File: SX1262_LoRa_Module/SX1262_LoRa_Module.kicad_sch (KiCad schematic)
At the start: 39 parts, among them J1 Conn_01x08_Pin, J2 Conn_01x10_Pin, J3 Conn_01x06_Pin, J4 Conn_01x08_Pin, Q1 32.0Mhz, U1 SX1262IMLTRT, U2 PE4259

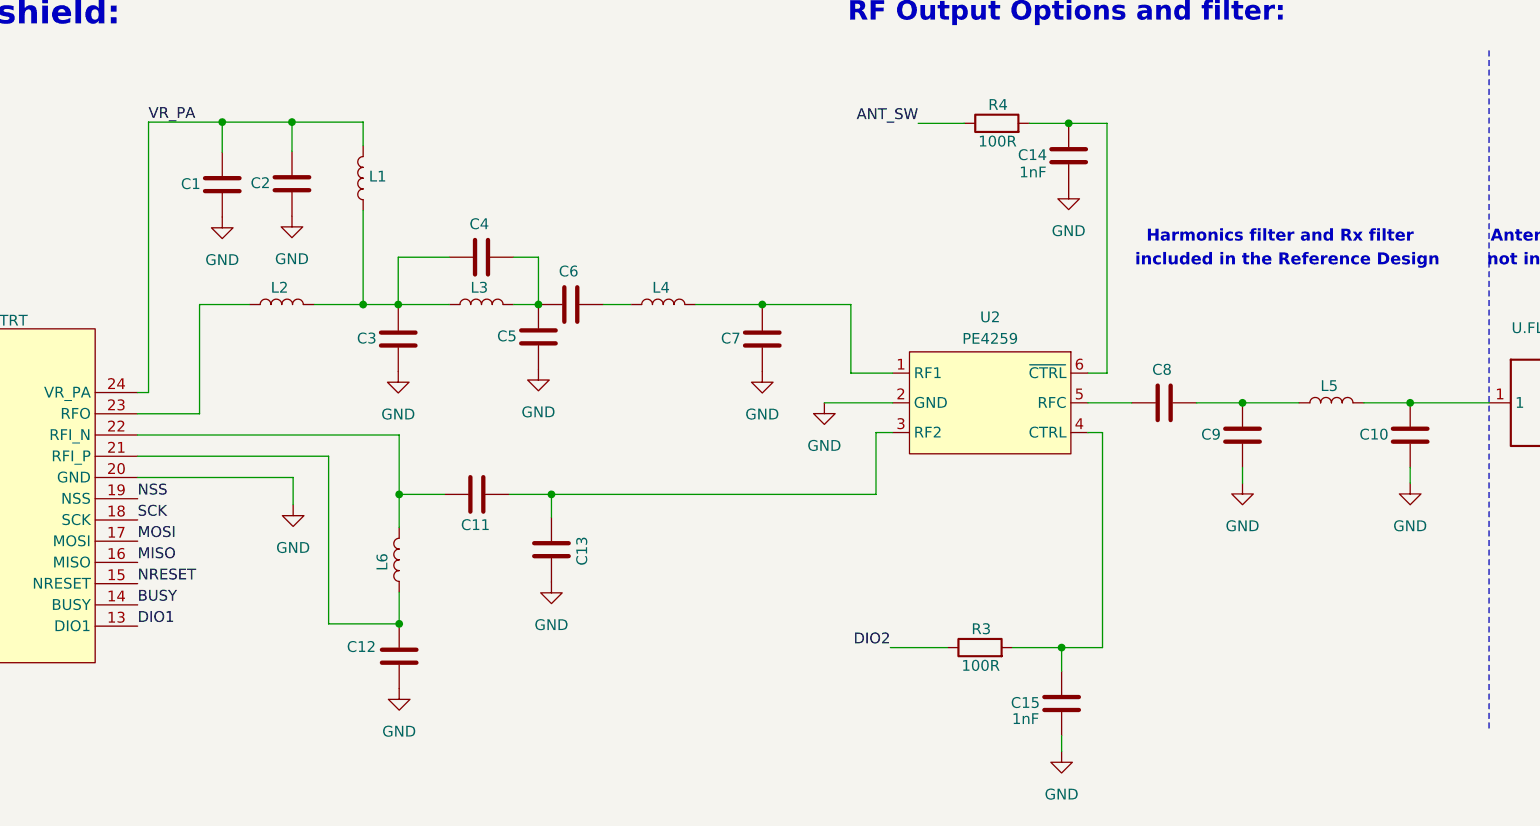
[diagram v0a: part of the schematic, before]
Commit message: -added LC value for the filters
- added values for LC filters based on SEMTECH BOM
- It is recommended to do an 0402 size for the components for the filters , thus following SEMTECH layout size
- Need to note that schemetic here doesnt have yet 0402 footprints designation still contemplating
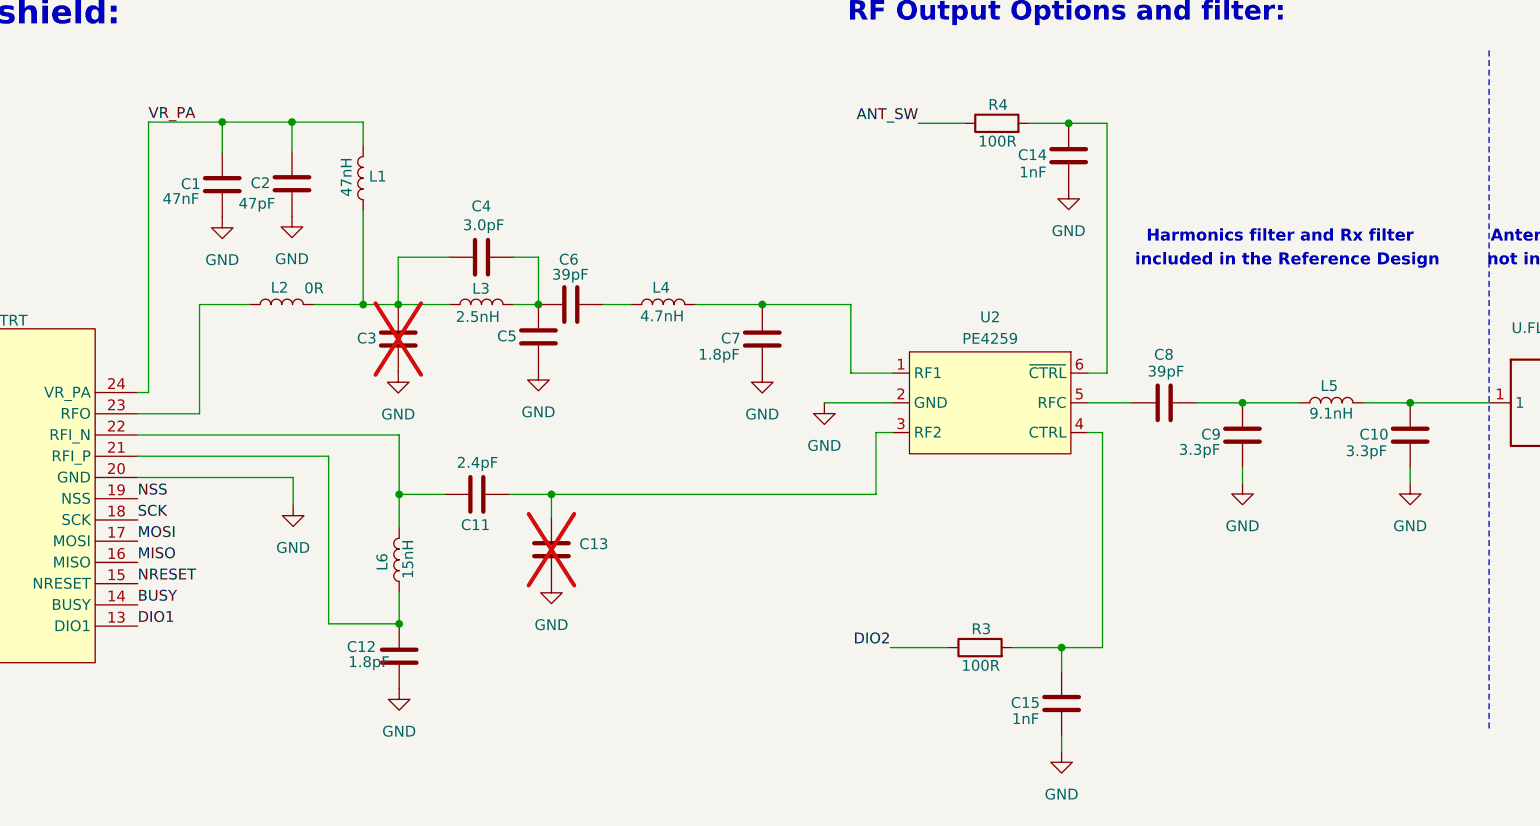
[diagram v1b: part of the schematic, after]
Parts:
- C1: value ~ -> 47nF
- C10, C9: value ~ -> 3.3pF
- C11: value ~ -> 2.4pF
- C12, C7: value ~ -> 1.8pF
- C13, C3: now not fitted
- C2: value ~ -> 47pF
- C4: value ~ -> 3.0pF
- C6, C8: value ~ -> 39pF
- L1: value ~ -> 47nH
- L2: value ~ -> 0R
- L3: value ~ -> 2.5nH
- L4: value ~ -> 4.7nH
- L5: value ~ -> 9.1nH
- L6: value ~ -> 15nH
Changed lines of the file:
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@@
 			)
 		)
-		(property "Value" "~"
+		(property "Value" "1.8pF"
 			(at 209.6668 122.5537 0)
 			(effects
@@
 			)
 		)
-		(property "Value" "~"
-			(at 320.9204 95.1531 0)
+		(property "Value" "3.3pF"
+			(at 312.3157 97.568 0)
 			(effects
 				(font
@@
 		(dnp no)
 		(property "Reference" "C8"
-			(at 304.2977 88.1389 90)
+			(at 304.5224 86.3721 90)
 			(effects
 				(font
@@
 			)
 		)
-		(property "Value" "~"
-			(at 305.0212 86.049 0)
+		(property "Value" "39pF"
+			(at 303.7605 88.3487 90)
 			(effects
 				(font
@@
 			)
 		)
-		(property "Value" "~"
-			(at 250.5509 78.5488 90)
+		(property "Value" "4.7nH"
+			(at 246.6076 81.8426 90)
 			(effects
 				(font
@@
 		(in_bom yes)
 		(on_board yes)
-		(dnp no)
+		(dnp yes)
 		(property "Reference" "C3"
 			(at 212.9982 84.4555 0)
@@
 		(dnp no)
 		(property "Reference" "C6"
-			(at 234.4421 76.5652 90)
+			(at 234.4594 75.1748 90)
 			(effects
 				(font
@@
 			)
 		)
-		(property "Value" "~"
-			(at 235.1656 74.4753 0)
+		(property "Value" "39pF"
+			(at 233.6358 76.9455 90)
 			(effects
 				(font
@@
 			)
 		)
-		(property "Value" "~"
-			(at 225.4841 108.7978 0)
+		(property "Value" "2.4pF"
+			(at 227.3103 99.092 90)
 			(effects
 				(font
@@
 			)
 		)
-		(property "Value" "~"
-			(at 213.7403 106.7047 90)
+		(property "Value" "15nH"
+			(at 216.7012 110.4423 90)
 			(effects
 				(font
@@
 			)
 		)
-		(property "Value" "~"
-			(at 340.6594 95.1531 0)
+		(property "Value" "3.3pF"
+			(at 331.9588 97.7224 0)
 			(effects
 				(font
@@
 			)
 		)
-		(property "Value" "~"
-			(at 200.8062 65.6565 0)
+		(property "Value" "47nF"
+			(at 192.1154 68.0237 0)
 			(effects
 				(font
@@
 		(dnp no)
 		(property "Reference" "L3"
-			(at 225.0829 78.479 90)
+			(at 225.2813 78.6048 90)
 			(effects
 				(font
@@
 			)
 		)
-		(property "Value" "~"
-			(at 229.1511 78.5488 90)
+		(property "Value" "2.5nH"
+			(at 224.9107 81.9198 90)
 			(effects
 				(font
@@
 		(dnp no)
 		(property "Reference" "C4"
-			(at 223.928 70.9967 90)
+			(at 224.1643 68.8948 90)
 			(effects
 				(font
@@
 			)
 		)
-		(property "Value" "~"
-			(at 224.6515 68.9068 0)
+		(property "Value" "3.0pF"
+			(at 223.1554 71.1185 90)
 			(effects
 				(font
@@
 			)
 		)
-		(property "Value" "~"
+		(property "Value" "0R"
 			(at 205.6345 78.5488 90)
 			(effects
@@
 			)
 		)
-		(property "Value" "~"
-			(at 209.0102 65.5485 0)
+		(property "Value" "47pF"
+			(at 201.0633 68.5835 0)
 			(effects
 				(font
@@
 			)
 		)
-		(property "Value" "~"
-			(at 264.3822 83.8365 0)
+		(property "Value" "1.8pF"
+			(at 255.7479 86.3612 0)
 			(effects
 				(font
@@
 		(in_bom yes)
 		(on_board yes)
-		(dnp no)
+		(dnp yes)
 		(property "Reference" "C13"
-			(at 237.1874 107.7624 90)
+			(at 240.2821 108.6664 0)
 			(effects
 				(font
@@
 			)
 		)
-		(property "Value" "~"
-			(at 329.2137 90.1225 90)
+		(property "Value" "9.1nH"
+			(at 325.3877 93.2988 90)
 			(effects
 				(font
@@
 			)
 		)
-		(property "Value" "~"
-			(at 209.4983 61.7701 90)
+		(property "Value" "47nH"
+			(at 209.4589 65.4648 90)
 			(effects
 				(font

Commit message: -layout update
- place footprint per component on schematic
- placed the components on pcb layout based on the evaluation board
- included shiled on the pcb placement
- placed routing on the pcb for the IC and rf switch
- remaining task to deliberate is 10 pins if its either castillated or header
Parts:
- C1, C10, C11, C12, C13, C14, C15, C16, C17, C18, C2, C3, C4, C6, C7, C8, C9: footprint (none) -> Capacitor_SMD:C_0402_1005Metric
- C20: footprint (none) -> Capacitor_SMD:C_0603_1608Metric
- C22: footprint (none) -> Capacitor_SMD:C_0805_2012Metric
- C23: value 10uF -> 100nF; footprint (none) -> Capacitor_SMD:C_0603_1608Metric
- C5: value ~ -> 5.6pF; footprint (none) -> Capacitor_SMD:C_0402_1005Metric
- L1: footprint (none) -> Inductor_SMD:L_0402_1005Metric; LCSC (none) -> C192855
- L2: footprint (none) -> Inductor_SMD:L_0402_1005Metric
- L3: footprint (none) -> Inductor_SMD:L_0402_1005Metric; LCSC (none) -> C703121
- L4: footprint (none) -> Inductor_SMD:L_0402_1005Metric; LCSC (none) -> C98064
- L5: footprint (none) -> Inductor_SMD:L_0402_1005Metric; LCSC (none) -> C6652904
- L6: footprint (none) -> Inductor_SMD:L_0402_1005Metric; LCSC (none) -> C91621
- L7: footprint (none) -> Lora_Footprint_Library:L0805; LCSC (none) -> C383402
- Q1: footprint (none) -> Lora_Footprint_Library:CRYSTAL-SMD_4P-L2.0-W1.6-BL; LCSC (none) -> C1986260
- R1: footprint (none) -> Resistor_SMD:R_0603_1608Metric
- R3, R4: footprint (none) -> Resistor_SMD:R_0402_1005Metric
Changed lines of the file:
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@@
 			)
 		)
-		(property "Footprint" ""
+		(property "Footprint" "Capacitor_SMD:C_0402_1005Metric"
 			(at 125.2082 122.1921 0)
 			(effects
@@
 		)
 		(property "Value" "1.8pF"
-			(at 209.6668 122.5537 0)
+			(at 207.68 122.7986 0)
 			(effects
 				(font
@@
 			)
 		)
-		(property "Footprint" ""
+		(property "Footprint" "Capacitor_SMD:C_0402_1005Metric"
 			(at 216.6157 125.6741 0)
 			(effects
@@
 			)
 		)
-		(property "Footprint" ""
+		(property "Footprint" "Capacitor_SMD:C_0402_1005Metric"
 			(at 313.9715 92.0327 0)
 			(effects
@@
 			)
 		)
-		(property "Footprint" ""
+		(property "Footprint" "Capacitor_SMD:C_0402_1005Metric"
 			(at 138.8917 82.3903 0)
 			(effects
@@
 			)
 		)
-		(property "Footprint" ""
+		(property "Footprint" "Capacitor_SMD:C_0402_1005Metric"
 			(at 301.9008 92.9979 0)
 			(effects
@@
 			)
 		)
-		(property "Footprint" ""
+		(property "Footprint" "Inductor_SMD:L_0402_1005Metric"
 			(at 246.7409 80.459 0)
 			(effects
@@
 			)
 		)
+		(property "LCSC" "C98064"
+			(at 246.7409 80.459 90)
+			(effects
+				(font
+					(size 1.27 1.27)
+				)
+				(hide yes)
+			)
+		)
 		(pin "2"
 		)
@@
 			)
 		)
-		(property "Footprint" ""
+		(property "Footprint" "Capacitor_SMD:C_0402_1005Metric"
 			(at 214.5764 80.7161 0)
 			(effects
@@
 			)
 		)
-		(property "Footprint" ""
+		(property "Footprint" "Capacitor_SMD:C_0402_1005Metric"
 			(at 232.0452 81.4242 0)
 			(effects
@@
 			)
 		)
-		(property "Footprint" ""
+		(property "Footprint" "Capacitor_SMD:C_0402_1005Metric"
 			(at 228.6045 101.8489 0)
 			(effects
@@
 			)
 		)
-		(property "Footprint" ""
+		(property "Footprint" "Capacitor_SMD:C_0402_1005Metric"
 			(at 113.0597 122.2721 0)
 			(effects
@@
 			)
 		)
-		(property "Footprint" ""
+		(property "Footprint" "Inductor_SMD:L_0402_1005Metric"
 			(at 215.6505 110.5147 0)
 			(effects
@@
 			)
 		)
+		(property "LCSC" "C91621"
+			(at 215.6505 110.5147 90)
+			(effects
+				(font
+					(size 1.27 1.27)
+				)
+				(hide yes)
+			)
+		)
 		(pin "2"
 		)
@@
 			)
 		)
-		(property "Footprint" ""
+		(property "Footprint" "Capacitor_SMD:C_0402_1005Metric"
 			(at 333.7105 92.0327 0)
 			(effects
@@
 			)
 		)
-		(property "Footprint" ""
+		(property "Footprint" "Capacitor_SMD:C_0402_1005Metric"
 			(at 193.8573 62.5361 0)
 			(effects
@@
 			)
 		)
-		(property "Footprint" ""
+		(property "Footprint" "Inductor_SMD:L_0402_1005Metric"
 			(at 225.3411 80.459 0)
 			(effects
@@
 			)
 		)
+		(property "LCSC" "C703121"
+			(at 225.3411 80.459 90)
+			(effects
+				(font
+					(size 1.27 1.27)
+				)
+				(hide yes)
+			)
+		)
 		(pin "2"
 		)
@@
 			)
 		)
-		(property "Footprint" ""
+		(property "Footprint" "Capacitor_SMD:C_0402_1005Metric"
 			(at 221.5311 75.8557 0)
 			(effects
@@
 			)
 		)
-		(property "Value" "~"
-			(at 238.0289 83.5794 0)
+		(property "Value" "5.6pF"
+			(at 229.3628 86.0393 0)
 			(effects
 				(font
@@
 			)
 		)
-		(property "Footprint" ""
+		(property "Footprint" "Capacitor_SMD:C_0402_1005Metric"
 			(at 231.08 80.459 0)
 			(effects
@@
 			)
 		)
-		(property "Footprint" ""
+		(property "Footprint" "Capacitor_SMD:C_0805_2012Metric"
 			(at 185.9707 220.9317 0)
 			(effects
@@
 			)
 		)
-		(property "Footprint" ""
+		(property "Footprint" "Inductor_SMD:L_0402_1005Metric"
 			(at 201.8245 80.459 0)
 			(effects
@@
 			)
 		)
-		(property "Footprint" ""
+		(property "Footprint" "Resistor_SMD:R_0402_1005Metric"
 			(at 284.0346 122.6261 90)
 			(effects
@@
 		(dnp no)
 		(property "Reference" "C23"
-			(at 189.1592 216.0317 0)
+			(at 189.2131 216.2264 0)
 			(effects
 				(font
@@
 			)
 		)
-		(property "Value" "10uF"
-			(at 188.2817 218.0114 0)
+		(property "Value" "100nF"
+			(at 187.1998 218.4215 0)
 			(effects
 				(font
@@
 			)
 		)
-		(property "Footprint" ""
+		(property "Footprint" "Capacitor_SMD:C_0603_1608Metric"
 			(at 196.286 220.9317 0)
 			(effects
@@
 			)
 		)
-		(property "Footprint" ""
+		(property "Footprint" "Capacitor_SMD:C_0402_1005Metric"
 			(at 202.0613 62.4281 0)
 			(effects
@@
 			)
 		)
-		(property "Footprint" ""
+		(property "Footprint" "Lora_Footprint_Library:L0805"
 			(at 124.3611 109.5967 0)
 			(effects
@@
 			)
 		)
+		(property "LCSC" "C383402"
+			(at 124.3611 109.5967 90)
+			(effects
+				(font
+					(size 1.27 1.27)
+				)
+				(hide yes)
+			)
+		)
 		(pin "2"
 		)
@@
 			)
 		)
-		(property "Footprint" ""
+		(property "Footprint" "Resistor_SMD:R_0603_1608Metric"
 			(at 209.3951 215.0897 90)
 			(effects
@@
 			)
 		)
-		(property "Footprint" ""
+		(property "Footprint" "Capacitor_SMD:C_0402_1005Metric"
 			(at 257.4333 80.7161 0)
 			(effects
@@
 			)
 		)
+		(property "LCSC" ""
+			(at 258.3985 84.5261 0)
+			(effects
+				(font
+					(size 1.27 1.27)
+				)
+				(hide yes)
+			)
+		)
 		(pin "2"
 		)
@@
 			)
 		)
-		(property "Footprint" ""
+		(property "Footprint" "Resistor_SMD:R_0402_1005Metric"
 			(at 286.0085 60.9041 90)
 			(effects
@@
 			)
 		)
-		(property "Footprint" ""
+		(property "Footprint" "Capacitor_SMD:C_0402_1005Metric"
 			(at 232.6111 105.5119 0)
 			(effects
@@
 			)
 		)
-		(property "Footprint" ""
+		(property "Footprint" "Capacitor_SMD:C_0402_1005Metric"
 			(at 292.6732 123.6219 0)
 			(effects
@@
 			)
 		)
-		(property "Footprint" ""
+		(property "Footprint" "Capacitor_SMD:C_0603_1608Metric"
 			(at 224.6013 220.9317 0)
 			(effects
@@
 			)
 		)
-		(property "Footprint" ""
+		(property "Footprint" "Inductor_SMD:L_0402_1005Metric"
 			(at 325.4037 92.0327 0)
 			(effects
@@
 			)
 		)
+		(property "LCSC" "C6652904"
+			(at 325.4037 92.0327 90)
+			(effects
+				(font
+					(size 1.27 1.27)
+				)
+				(hide yes)
+			)
+		)
 		(pin "2"
 		)
@@
 			)
 		)
-		(property "Footprint" ""
+		(property "Footprint" "Inductor_SMD:L_0402_1005Metric"
 			(at 211.4085 65.5801 0)
 			(effects
@@
 			)
 		)
+		(property "LCSC" "C192855"
+			(at 211.4085 65.5801 0)
+			(effects
+				(font
+					(size 1.27 1.27)
+				)
+				(hide yes)
+			)
+		)
 		(pin "2"
 		)
@@
 			)
 		)
-		(property "Footprint" ""
+		(property "Footprint" "Capacitor_SMD:C_0402_1005Metric"
 			(at 293.5039 59.1261 0)
 			(effects
@@
 			)
 		)
+		(property "Field5" ""
+			(at 294.4691 62.9361 0)
+			(effects
+				(font
+					(size 1.27 1.27)
+				)
+				(hide yes)
+			)
+		)
 		(pin "2"
 		)
@@
 			)
 		)
-		(property "Footprint" ""
+		(property "Footprint" "Lora_Footprint_Library:CRYSTAL-SMD_4P-L2.0-W1.6-BL"
 			(at 117.9616 65.9881 0)
 			(effects
@@
 			(at 117.9616 65.9881 0)
 			(effects
+				(font
+					(size 1.27 1.27)
+				)
+				(hide yes)
+			)
+		)
+		(property "LCSC" "C1986260"
+			(at 117.9616 65.9881 0)
+			(effects

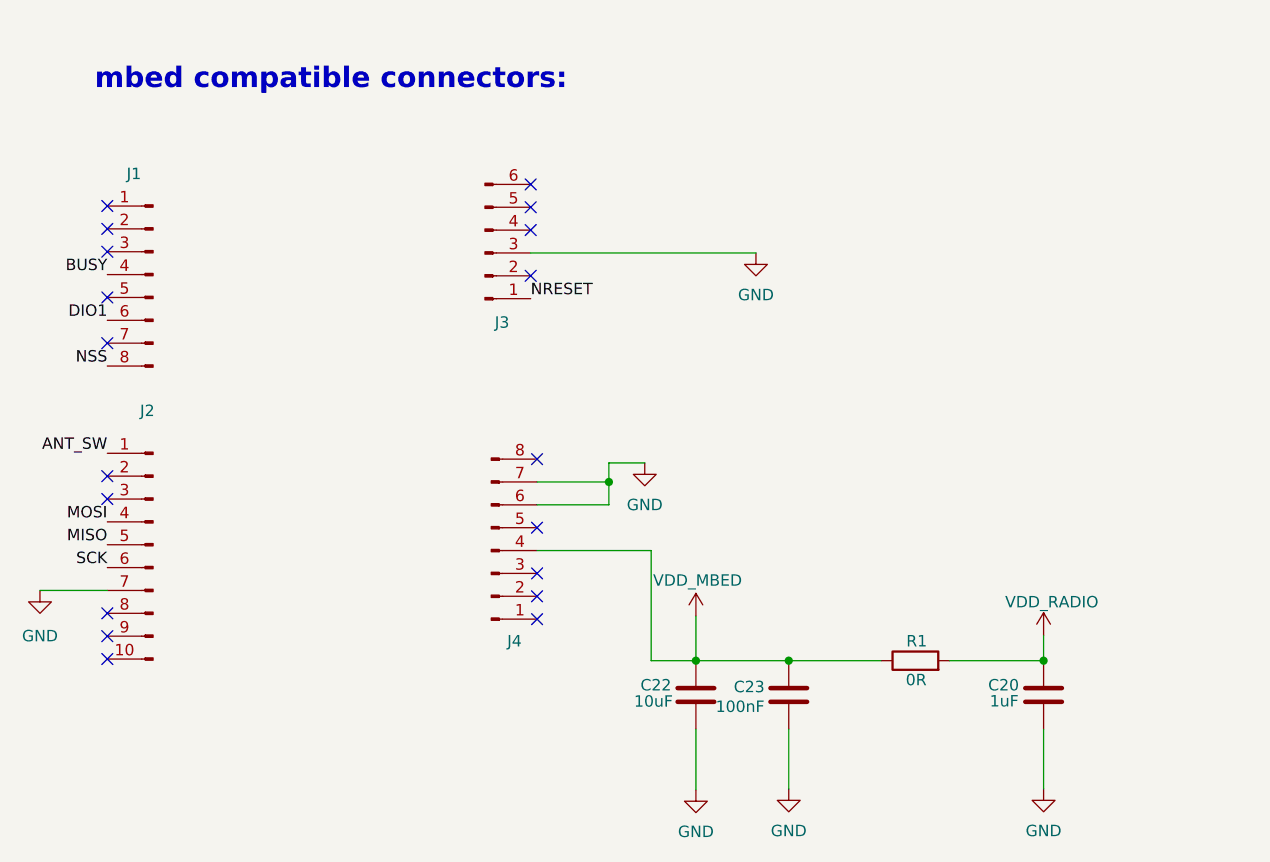
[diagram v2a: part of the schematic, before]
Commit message: -pcb
-done pcb routing
-including castellated pads
-warnings and error is due to tight placement of the components for the filter and tuning
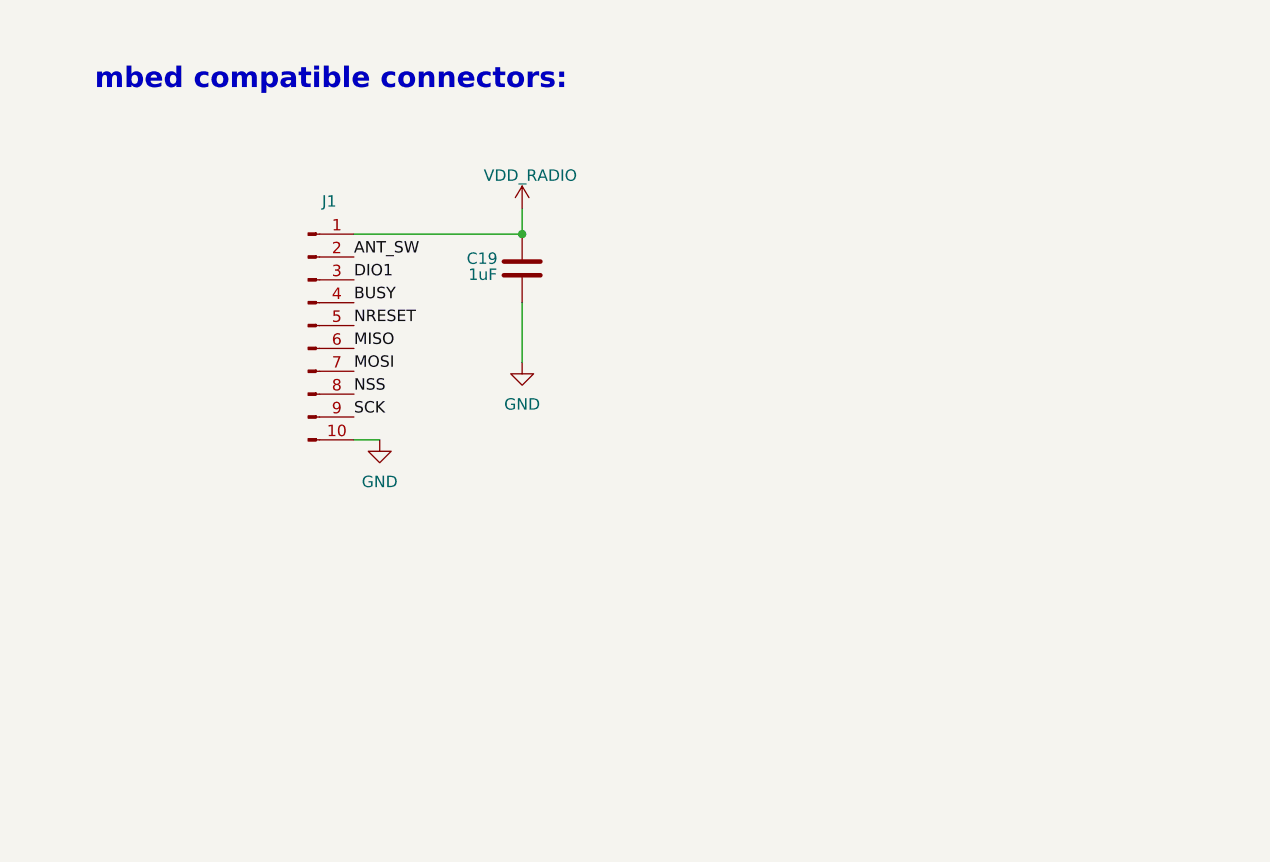
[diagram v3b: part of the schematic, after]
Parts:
- removed C20: 1uF, Capacitor_SMD:C_0603_1608Metric, symbol Device:C
- removed C22: 10uF, Capacitor_SMD:C_0805_2012Metric, symbol Device:C
- removed C23: 100nF, Capacitor_SMD:C_0603_1608Metric, symbol Device:C
- removed J1, J4: Conn_01x08_Pin, symbol Connector:Conn_01x08_Pin
- removed J2: Conn_01x10_Pin, symbol Connector:Conn_01x10_Pin
- removed J3: Conn_01x06_Pin, symbol Connector:Conn_01x06_Pin
- removed R1: 0R, Resistor_SMD:R_0603_1608Metric, symbol Device:R
- added C19: 1uF, Capacitor_SMD:C_0603_1608Metric, symbol Device:C
- added J1: Conn_01x10_Pin, Connector_PinHeader_2.54mm:PinHeader_1x10_P2.54mm_Vertical, symbol Connector:Conn_01x10_Pin
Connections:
- net ANT_SW: now also J1.2 (Pin_2)
- net BUSY: now also J1.4 (Pin_4)
- net DIO1: now also J1.3 (Pin_3)
- net GND: now also C19.2, J1.10 (Pin_10)
- net MISO: now also J1.6 (Pin_6)
- net MOSI: now also J1.7 (Pin_7)
- net NRESET: now also J1.5 (Pin_5)
- net NSS: now also J1.8 (Pin_8)
- net SCK: now also J1.9 (Pin_9)
- net VDD_RADIO: now also C19.1, J1.1 (Pin_1)
- no-connect marks 19 -> 0
